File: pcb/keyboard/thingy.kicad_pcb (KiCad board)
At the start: 2 copper layers, 226.7 x 54 mm, 47 parts, among them J1 Conn_02x09_Odd_Even, J10 Conn_01x04_Socket, J11 Conn_01x06_Pin, J12 Conn_01x06_Pin, J14 Conn_01x04_Socket, J16 Conn_01x04_MountingPin, J2 Conn_01x02_Socket, J3 Conn_01x02_Socket, J4 Conn_01x02_Socket, J5 Raspberry_Pi_2_3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

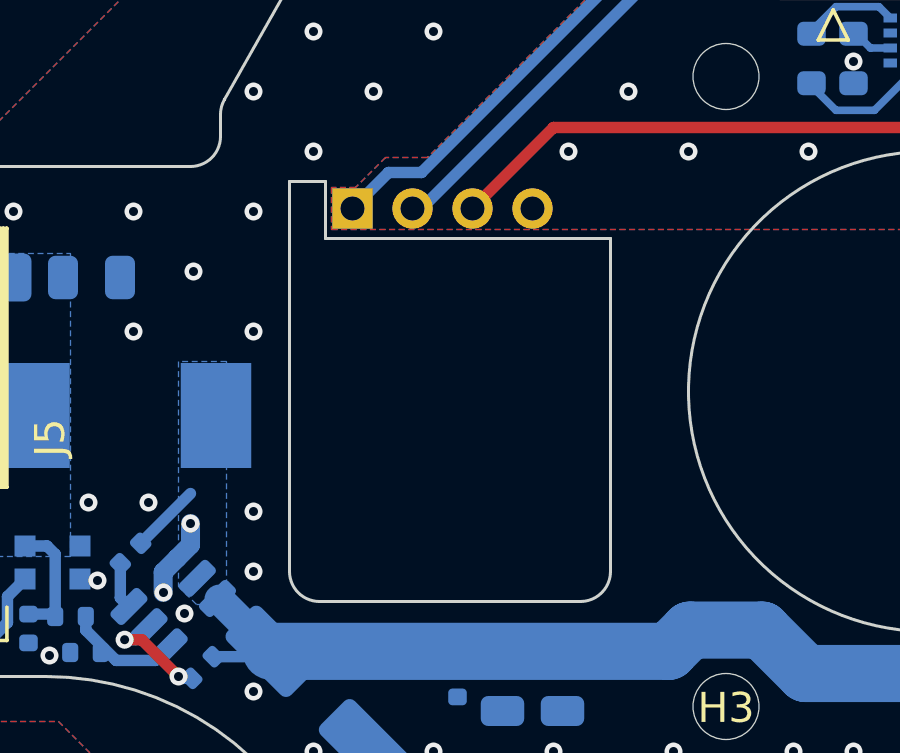
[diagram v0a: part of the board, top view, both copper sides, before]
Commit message: placement verification
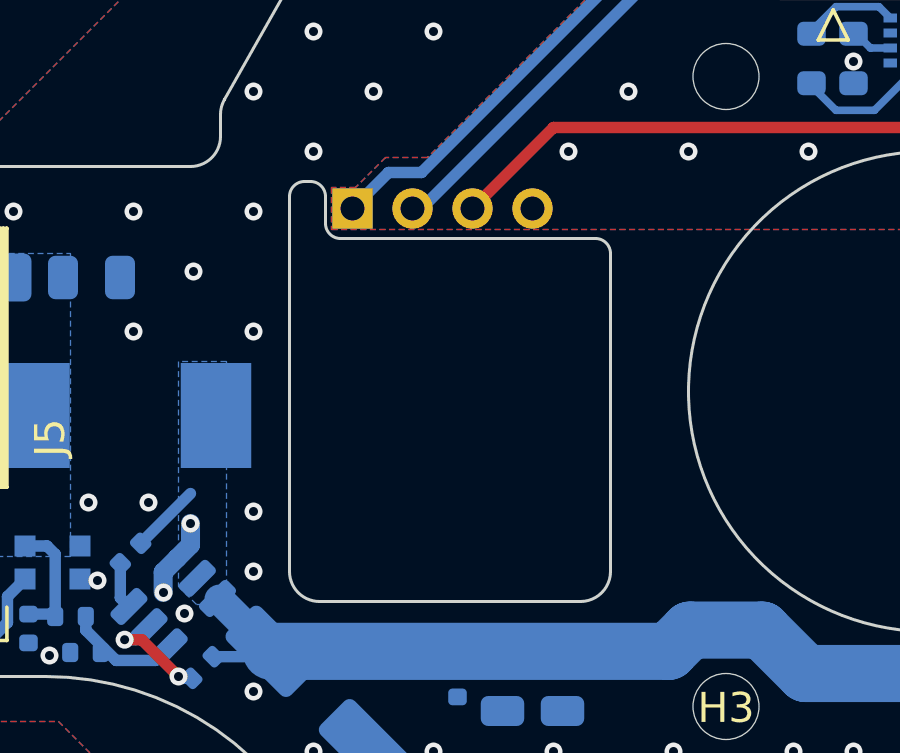
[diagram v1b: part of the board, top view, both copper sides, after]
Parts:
- C1: value C -> 100n
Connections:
- J9 pad 2: unconnected-(J9-Pin_2-Pad2) -> -BATT
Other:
- outline, holes or cut-outs redrawn
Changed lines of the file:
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@@
   (net 72 "Net-(J7-Pin_3)")
   (net 73 "Net-(J7-Pin_7)")
-  (net 74 "unconnected-(J9-Pin_2-Pad2)")
-  (net 75 "+3.3VP")
-  (net 76 "/SDA_P")
-  (net 77 "/SCL_P")
+  (net 74 "+3.3VP")
+  (net 75 "/SDA_P")
+  (net 76 "/SCL_P")
   (footprint "Connector_TE-Connectivity:TE_Micro-MaTch_215079-6_2x03_P1.27mm_Vertical" (layer "F.Cu")
     (at -3.175 -14.5475 90)
@@
       (stroke (width 0.1) (type solid)) (layer "F.Fab"))
     (pad "1" thru_hole circle (at 0 0 270) (size 1.7 1.7) (drill 1) (layers "*.Cu" "*.Mask")
-      (net 75 "+3.3VP") (pinfunction "3V3") (pintype "power_in"))
+      (net 74 "+3.3VP") (pinfunction "3V3") (pintype "power_in"))
     (pad "2" thru_hole oval (at -2.54 0 270) (size 1.7 1.7) (drill 1) (layers "*.Cu" "*.Mask")
       (net 7 "+5P") (pinfunction "5V") (pintype "power_in"))
     (pad "3" thru_hole oval (at 0 2.54 270) (size 1.7 1.7) (drill 1) (layers "*.Cu" "*.Mask")
-      (net 76 "/SDA_P") (pinfunction "SDA/GPIO2") (pintype "bidirectional"))
+      (net 75 "/SDA_P") (pinfunction "SDA/GPIO2") (pintype "bidirectional"))
     (pad "4" thru_hole oval (at -2.54 2.54 270) (size 1.7 1.7) (drill 1) (layers "*.Cu" "*.Mask")
       (net 7 "+5P") (pinfunction "5V") (pintype "power_in"))
     (pad "5" thru_hole oval (at 0 5.08 270) (size 1.7 1.7) (drill 1) (layers "*.Cu" "*.Mask")
-      (net 77 "/SCL_P") (pinfunction "SCL/GPIO3") (pintype "bidirectional"))
+      (net 76 "/SCL_P") (pinfunction "SCL/GPIO3") (pintype "bidirectional"))
     (pad "6" thru_hole oval (at -2.54 5.08 270) (size 1.7 1.7) (drill 1) (layers "*.Cu" "*.Mask")
       (net 8 "-BATT") (pinfunction "GND") (pintype "power_in"))
@@
       (net 46 "unconnected-(J9-Pin_1-Pad1)") (pinfunction "Pin_1") (pintype "passive"))
     (pad "2" smd roundrect (at -1.5 2) (size 0.6 1.55) (layers "B.Cu" "B.Paste" "B.Mask") (roundrect_rratio 0.25)
-      (net 74 "unconnected-(J9-Pin_2-Pad2)") (pinfunction "Pin_2") (pintype "passive"))
+      (net 8 "-BATT") (pinfunction "Pin_2") (pintype "passive"))
     (pad "3" smd roundrect (at -0.5 2) (size 0.6 1.55) (layers "B.Cu" "B.Paste" "B.Mask") (roundrect_rratio 0.25)
       (net 45 "/R1") (pinfunction "Pin_3") (pintype "passive"))
@@
       (stroke (width 0.1) (type solid)) (layer "B.Fab"))
     (pad "1" smd roundrect (at -1.5 -1.325) (size 0.6 1.55) (layers "B.Cu" "B.Paste" "B.Mask") (roundrect_rratio 0.25)
-      (net 77 "/SCL_P") (pinfunction "Pin_1") (pintype "passive"))
+      (net 76 "/SCL_P") (pinfunction "Pin_1") (pintype "passive"))
     (pad "2" smd roundrect (at -0.5 -1.325) (size 0.6 1.55) (layers "B.Cu" "B.Paste" "B.Mask") (roundrect_rratio 0.25)
-      (net 76 "/SDA_P") (pinfunction "Pin_2") (pintype "passive"))
+      (net 75 "/SDA_P") (pinfunction "Pin_2") (pintype "passive"))
     (pad "3" smd roundrect (at 0.5 -1.325) (size 0.6 1.55) (layers "B.Cu" "B.Paste" "B.Mask") (roundrect_rratio 0.25)
-      (net 75 "+3.3VP") (pinfunction "Pin_3") (pintype "passive"))
+      (net 74 "+3.3VP") (pinfunction "Pin_3") (pintype "passive"))
     (pad "4" smd roundrect (at 1.5 -1.325) (size 0.6 1.55) (layers "B.Cu" "B.Paste" "B.Mask") (roundrect_rratio 0.25)
       (net 8 "-BATT") (pinfunction "Pin_4") (pintype "passive"))
@@
         (effects (font (size 1 1) (thickness 0.15)) (justify mirror))
     )
-    (fp_text value "C" (at 0 -1.16 45) (layer "B.Fab") hide
+    (fp_text value "100n" (at 0 -1.16 45) (layer "B.Fab") hide
         (effects (font (size 1 1) (thickness 0.15)) (justify mirror))
     )
@@
   (gr_arc (start -19.649172 -16.47205) (mid -18.18301 -17.956024) (end -16.169083 -18.5)
     (stroke (width 0.1) (type default)) (layer "Edge.Cuts"))
-  (gr_line (start -20.1 -5.1) (end -10.6 -5.1)
+  (gr_line (start -19.6 -5.1) (end -11.1 -5.1)
     (stroke (width 0.1) (type default)) (layer "Edge.Cuts"))
   (gr_line (start -64.692893 10.607107) (end -65.507107 9.792893)
@@
   (gr_line (start -7.5 23) (end -7.5 22.5)
     (stroke (width 0.1) (type default)) (layer "Edge.Cuts"))
-  (gr_line (start -21.3 -7) (end -20.1 -7)
+  (gr_line (start -20.8 -7) (end -20.6 -7)
     (stroke (width 0.1) (type default)) (layer "Edge.Cuts"))
   (gr_line (start -82.6 -4) (end -84.6 -4)
@@
   (gr_line (start 104.35 -26) (end 104.35 -10.742641)
     (stroke (width 0.1) (type default)) (layer "Edge.Cuts"))
+  (gr_arc (start -21.3 -6.5) (mid -21.153553 -6.853553) (end -20.8 -7)
+    (stroke (width 0.1) (type default)) (layer "Edge.Cuts"))
   (gr_line (start 3.5 27) (end -3.5 27)
     (stroke (width 0.1) (type default)) (layer "Edge.Cuts"))
   (gr_arc (start 11.5 -18.5) (mid 8.671573 -19.671573) (end 7.5 -22.5)
     (stroke (width 0.1) (type default)) (layer "Edge.Cuts"))
+  (gr_arc (start -11.1 -5.1) (mid -10.746447 -4.953553) (end -10.6 -4.6)
+    (stroke (width 0.1) (type default)) (layer "Edge.Cuts"))
   (gr_line (start 31.156854 7.5) (end 31.5 7.5)
     (stroke (width 0.1) (type default)) (layer "Edge.Cuts"))
   (gr_arc (start -63.985786 10.9) (mid -64.36847 10.82388) (end -64.692893 10.607107)
     (stroke (width 0.1) (type default)) (layer "Edge.Cuts"))
-  (gr_line (start -20.1 -7) (end -20.1 -5.1)
+  (gr_line (start -20.1 -6.5) (end -20.1 -5.6)
     (stroke (width 0.1) (type default)) (layer "Edge.Cuts"))
   (gr_arc (start -84.6 4) (mid -85.307107 3.707107) (end -85.6 3)
@@
   (gr_arc (start 117.892641 6.8) (mid 116.744591 6.571639) (end 115.771321 5.921321)
     (stroke (width 0.1) (type default)) (layer "Edge.Cuts"))
+  (gr_arc (start -19.6 -5.1) (mid -19.953553 -5.246447) (end -20.1 -5.6)
+    (stroke (width 0.1) (type default)) (layer "Edge.Cuts"))
   (gr_line (start -79.1 -7.5) (end -24.6 -7.5)
     (stroke (width 0.1) (type default)) (layer "Edge.Cuts"))
@@
   (gr_arc (start -20.300001 7) (mid -21.007107 6.707107) (end -21.3 6)
     (stroke (width 0.1) (type default)) (layer "Edge.Cuts"))
-  (gr_line (start -10.6 -5.1) (end -10.6 6)
+  (gr_line (start -10.6 -4.6) (end -10.6 6)
     (stroke (width 0.1) (type default)) (layer "Edge.Cuts"))
   (gr_line (start 16.843146 18.5) (end 11.5 18.5)
@@
   (gr_arc (start -7.5 -22.5) (mid -8.671573 -19.671573) (end -11.5 -18.5)
     (stroke (width 0.1) (type default)) (layer "Edge.Cuts"))
-  (gr_line (start -21.3 6) (end -21.3 -7)
+  (gr_line (start -21.3 6) (end -21.3 -6.5)
     (stroke (width 0.1) (type default)) (layer "Edge.Cuts"))
   (gr_arc (start 31.156854 -7.5) (mid 29.62612 -7.804482) (end 28.328427 -8.671573)
@@
   (gr_arc (start -79.1 9.5) (mid -80.867767 8.767767) (end -81.6 7)
     (stroke (width 0.1) (type default)) (layer "Edge.Cuts"))
+  (gr_arc (start -20.6 -7) (mid -20.246447 -6.853553) (end -20.1 -6.5)
+    (stroke (width 0.1) (type default)) (layer "Edge.Cuts"))
   (gr_text "USE ONLY SEEEDUINO\nXIAO ESP32-C6/S3" (at -57.4 1) (layer "B.SilkS")
     (effects (font (size 1 1) (thickness 0.15)) (justify bottom mirror))
@@
   (segment (start 117.085 10.72) (end 139.975 10.72) (width 0.635) (layer "B.Cu") (net 70))
   (segment (start 107.63 1.265) (end 117.085 10.72) (width 0.635) (layer "B.Cu") (net 70))
-  (segment (start -36.385668 1.1) (end -33.3 4.185668) (width 0.381) (layer "F.Cu") (net 75))
-  (segment (start -33.3 4.185668) (end -33.3 5.94) (width 0.381) (layer "F.Cu") (net 75))
-  (segment (start -37.2 1.1) (end -36.385668 1.1) (width 0.381) (layer "F.Cu") (net 75))
-  (segment (start -33.3 5.94) (end -32.05 7.19) (width 0.381) (layer "F.Cu") (net 75))
-  (via (at -37.2 1.1) (size 0.6) (drill 0.3) (layers "F.Cu" "B.Cu") (net 75))
-  (segment (start -37.2 1.1) (end -37.7 0.6) (width 0.381) (layer "B.Cu") (net 75))
-  (segment (start -37.7 0.6) (end -37.7 -0.125) (width 0.381) (layer "B.Cu") (net 75))
-  (segment (start -35.8305 3.975866) (end -35.8305 5.9495) (width 0.381) (layer "B.Cu") (net 76))
-  (segment (start -35.8305 5.9495) (end -34.59 7.19) (width 0.381) (layer "B.Cu") (net 76))
-  (segment (start -38.7 -0.225) (end -38.7 1.106366) (width 0.381) (layer "B.Cu") (net 76))
-  (segment (start -38.7 1.106366) (end -35.8305 3.975866) (width 0.381) (layer "B.Cu") (net 76))
-  (segment (start -39.7 0.96561) (end -38.4 2.26561) (width 0.381) (layer "B.Cu") (net 77))
-  (segment (start -39.7 -0.225) (end -39.7 0.96561) (width 0.381) (layer "B.Cu") (net 77))
-  (segment (start -38.4 2.26561) (end -38.4 5.92) (width 0.381) (layer "B.Cu") (net 77))
-  (segment (start -38.4 5.92) (end -37.13 7.19) (width 0.381) (layer "B.Cu") (net 77))
+  (segment (start -36.385668 1.1) (end -33.3 4.185668) (width 0.381) (layer "F.Cu") (net 74))
+  (segment (start -33.3 4.185668) (end -33.3 5.94) (width 0.381) (layer "F.Cu") (net 74))
+  (segment (start -37.2 1.1) (end -36.385668 1.1) (width 0.381) (layer "F.Cu") (net 74))
+  (segment (start -33.3 5.94) (end -32.05 7.19) (width 0.381) (layer "F.Cu") (net 74))
+  (via (at -37.2 1.1) (size 0.6) (drill 0.3) (layers "F.Cu" "B.Cu") (net 74))
+  (segment (start -37.2 1.1) (end -37.7 0.6) (width 0.381) (layer "B.Cu") (net 74))
+  (segment (start -37.7 0.6) (end -37.7 -0.125) (width 0.381) (layer "B.Cu") (net 74))
+  (segment (start -35.8305 3.975866) (end -35.8305 5.9495) (width 0.381) (layer "B.Cu") (net 75))
+  (segment (start -35.8305 5.9495) (end -34.59 7.19) (width 0.381) (layer "B.Cu") (net 75))
+  (segment (start -38.7 -0.225) (end -38.7 1.106366) (width 0.381) (layer "B.Cu") (net 75))
+  (segment (start -38.7 1.106366) (end -35.8305 3.975866) (width 0.381) (layer "B.Cu") (net 75))
+  (segment (start -39.7 0.96561) (end -38.4 2.26561) (width 0.381) (layer "B.Cu") (net 76))
+  (segment (start -39.7 -0.225) (end -39.7 0.96561) (width 0.381) (layer "B.Cu") (net 76))
+  (segment (start -38.4 2.26561) (end -38.4 5.92) (width 0.381) (layer "B.Cu") (net 76))
+  (segment (start -38.4 5.92) (end -37.13 7.19) (width 0.381) (layer "B.Cu") (net 76))
   (zone (net 8) (net_name "-BATT") (layer "F.Cu") (hatch edge 0.5)
     (connect_pads yes (clearance 0.5))
